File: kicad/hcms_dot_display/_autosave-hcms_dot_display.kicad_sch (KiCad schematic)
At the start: 40 parts, among them J1 Conn_01x11, J2 USB_C_Receptacle_USB2.0, J3 Conn_01x11, J4 Conn_01x10_Female, J5 Conn_01x10_Male, Q1 Q_PMOS_DSG, Q2 Q_PMOS_DSG, Q3 Q_PMOS_DSG, Q4 Q_PMOS_DSG, Q5 Q_PMOS_DSG, SW2 SW_SPST, U1 ATtiny824-SSF, U2 FT231XS

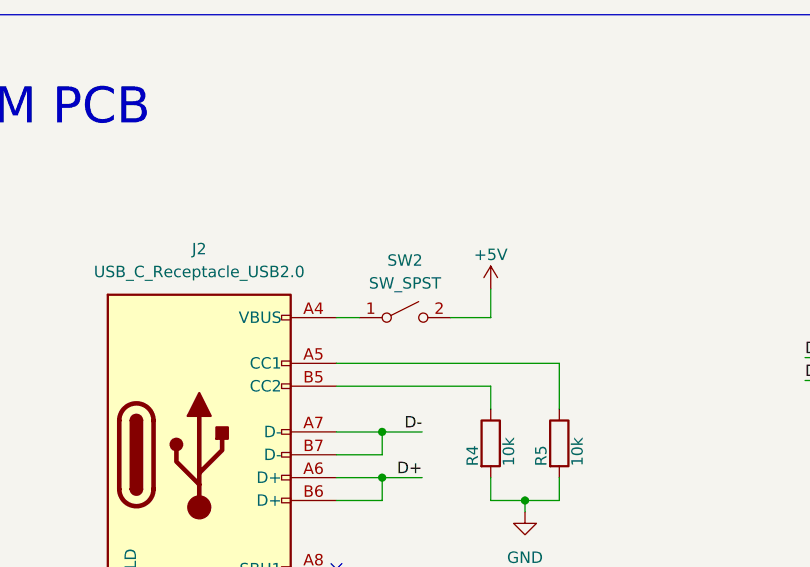
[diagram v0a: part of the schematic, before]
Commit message: 3d model environment variables lol
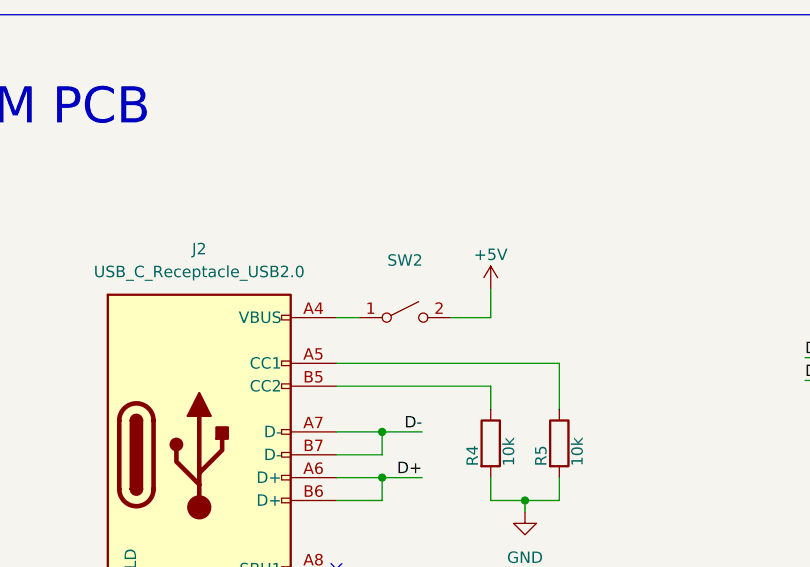
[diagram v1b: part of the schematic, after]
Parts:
- SW2: value SW_SPST -> (none)
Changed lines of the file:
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@@
     (in_bom yes) (on_board yes) (fields_autoplaced)
     (property "Reference" "SW2" (id 0) (at 84.455 187.325 0))
-    (property "Value" "SW_SPST" (id 1) (at 84.455 189.865 0))
+    (property "Value" "" (id 1) (at 84.455 189.865 0))
     (property "Footprint" "" (id 2) (at 84.455 193.675 0)
       (effects (font (size 1.27 1.27)) hide)
@@
     )
     (path "/8d1441a6-821f-419f-9338-76f0317eb8c7"
-      (reference "SW2") (unit 1) (value "SW_SPST") (footprint "")
+      (reference "SW2") (unit 1) (value "SW_SPST") (footprint "Button_Switch_SMD:SW_DIP_SPSTx03_Slide_KingTek_DSHP03TS_W7.62mm_P1.27mm")
     )
     (path "/74b91311-c571-4be4-b48f-44583fe63ca4"
